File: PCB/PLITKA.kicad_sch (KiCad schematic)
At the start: 47 parts, among them SW1 SW_DPDT_x2, SW10 MX_SW_HS, SW11 MX_SW_HS, SW12 MX_SW_HS, SW13 MX_SW_HS, SW14 MX_SW_HS, SW15 MX_SW_HS, SW16 MX_SW_HS, SW17 MX_SW_HS, SW18 MX_SW_HS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

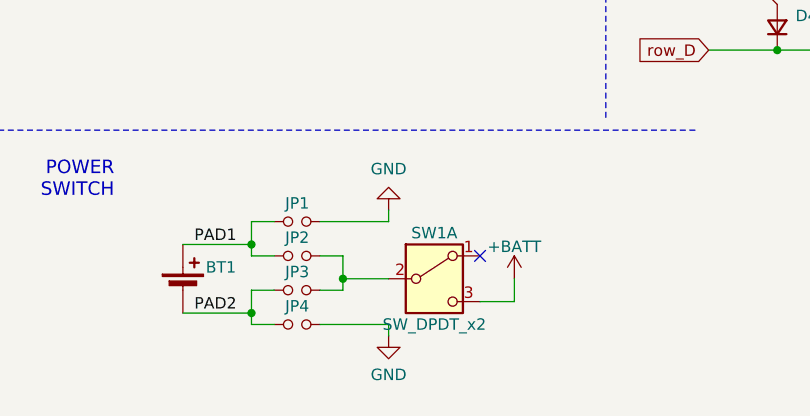
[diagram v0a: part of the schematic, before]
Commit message: ERC warning resolution, added the second pole-part for the double sided power switch
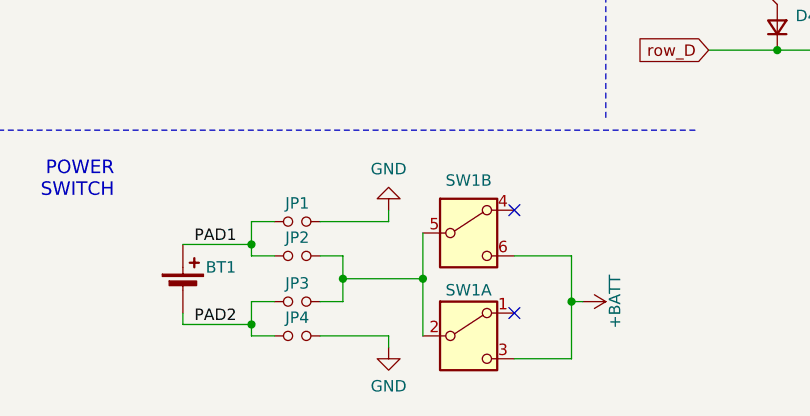
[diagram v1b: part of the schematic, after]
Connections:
- net +BATT: now also SW1.6 (C)
- net at JP2.2, JP3.2, SW1.2 (B): now also SW1.5 (B)
- no-connect marks 13 -> 14
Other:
- moved on the sheet: JP3, JP4, SW1B
